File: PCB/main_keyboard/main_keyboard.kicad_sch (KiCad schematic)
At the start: 160 parts

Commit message: Added virtual rows to key matrix #6
The "vritual" rows reduce GPIO usage with matrix from (5+16=21) to (10+8=18)
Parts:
- removed D20, D33, D34, D35, D38, D46, D51, D56, D61, D67, D78, D79: Diode, symbol ScottoKeebs:Placeholder_Diode
- removed S20, S33, S34, S35, S38, S46, S51, S56, S61, S67, S78, S79: Keyswitch, symbol ScottoKeebs:Placeholder_Keyswitch
- D1, D2, D3, D4, D5: footprint (none) -> ScottoKeebs_Components:Diode_DO-35
- D10: renamed from D45; footprint (none) -> ScottoKeebs_Components:Diode_DO-35
- D11: renamed from D6; footprint (none) -> ScottoKeebs_Components:Diode_DO-35
- D12: renamed from D7; footprint (none) -> ScottoKeebs_Components:Diode_DO-35
- D13: renamed from D8; footprint (none) -> ScottoKeebs_Components:Diode_DO-35
- D14: renamed from D9; footprint (none) -> ScottoKeebs_Components:Diode_DO-35
- D15: renamed from D10; footprint (none) -> ScottoKeebs_Components:Diode_DO-35
- D16: renamed from D47; footprint (none) -> ScottoKeebs_Components:Diode_DO-35
- D17: renamed from D48; footprint (none) -> ScottoKeebs_Components:Diode_DO-35
- D18: renamed from D49; footprint (none) -> ScottoKeebs_Components:Diode_DO-35
- D19: renamed from D50; footprint (none) -> ScottoKeebs_Components:Diode_DO-35
- D20: renamed from D11; footprint (none) -> ScottoKeebs_Components:Diode_DO-35
- D21: renamed from D12; footprint (none) -> ScottoKeebs_Components:Diode_DO-35
- D22: renamed from D13; footprint (none) -> ScottoKeebs_Components:Diode_DO-35
- D23: renamed from D14; footprint (none) -> ScottoKeebs_Components:Diode_DO-35
- D24: renamed from D15; footprint (none) -> ScottoKeebs_Components:Diode_DO-35
- D25: renamed from D52; footprint (none) -> ScottoKeebs_Components:Diode_DO-35
- D26: renamed from D53; footprint (none) -> ScottoKeebs_Components:Diode_DO-35
- D27: renamed from D54; footprint (none) -> ScottoKeebs_Components:Diode_DO-35
- D28: renamed from D55; footprint (none) -> ScottoKeebs_Components:Diode_DO-35
- D29: renamed from D16; footprint (none) -> ScottoKeebs_Components:Diode_DO-35
- D30: renamed from D17; footprint (none) -> ScottoKeebs_Components:Diode_DO-35
- D31: renamed from D18; footprint (none) -> ScottoKeebs_Components:Diode_DO-35
- D32: renamed from D19; footprint (none) -> ScottoKeebs_Components:Diode_DO-35
- D33: renamed from D57; footprint (none) -> ScottoKeebs_Components:Diode_DO-35
- D34: renamed from D58; footprint (none) -> ScottoKeebs_Components:Diode_DO-35
- D35: renamed from D59; footprint (none) -> ScottoKeebs_Components:Diode_DO-35
- D36: renamed from D60; footprint (none) -> ScottoKeebs_Components:Diode_DO-35
- D37: renamed from D21; footprint (none) -> ScottoKeebs_Components:Diode_DO-35
- D38: renamed from D22; footprint (none) -> ScottoKeebs_Components:Diode_DO-35
- D39: renamed from D23; footprint (none) -> ScottoKeebs_Components:Diode_DO-35
- D40: renamed from D24; footprint (none) -> ScottoKeebs_Components:Diode_DO-35
- D41: renamed from D25; footprint (none) -> ScottoKeebs_Components:Diode_DO-35
- D42: renamed from D62; footprint (none) -> ScottoKeebs_Components:Diode_DO-35
- D43: renamed from D63; footprint (none) -> ScottoKeebs_Components:Diode_DO-35
- D44: renamed from D64; footprint (none) -> ScottoKeebs_Components:Diode_DO-35
- D45: renamed from D65; footprint (none) -> ScottoKeebs_Components:Diode_DO-35
- D46: renamed from D26; footprint (none) -> ScottoKeebs_Components:Diode_DO-35
- D47: renamed from D27; footprint (none) -> ScottoKeebs_Components:Diode_DO-35
- D48: renamed from D28; footprint (none) -> ScottoKeebs_Components:Diode_DO-35
- D49: renamed from D29; footprint (none) -> ScottoKeebs_Components:Diode_DO-35
- D50: renamed from D30; footprint (none) -> ScottoKeebs_Components:Diode_DO-35
- D51: renamed from D66; footprint (none) -> ScottoKeebs_Components:Diode_DO-35
- D52: renamed from D68; footprint (none) -> ScottoKeebs_Components:Diode_DO-35
- D53: renamed from D69; footprint (none) -> ScottoKeebs_Components:Diode_DO-35
- D54: renamed from D70; footprint (none) -> ScottoKeebs_Components:Diode_DO-35
- D55: renamed from D31; footprint (none) -> ScottoKeebs_Components:Diode_DO-35
- D56: renamed from D32; footprint (none) -> ScottoKeebs_Components:Diode_DO-35
- D57: renamed from D71; footprint (none) -> ScottoKeebs_Components:Diode_DO-35
- D58: renamed from D72; footprint (none) -> ScottoKeebs_Components:Diode_DO-35
- D59: renamed from D73; footprint (none) -> ScottoKeebs_Components:Diode_DO-35
- D6: renamed from D41; footprint (none) -> ScottoKeebs_Components:Diode_DO-35
- D60: renamed from D74; footprint (none) -> ScottoKeebs_Components:Diode_DO-35
- D61: renamed from D75; footprint (none) -> ScottoKeebs_Components:Diode_DO-35
- D62: renamed from D36; footprint (none) -> ScottoKeebs_Components:Diode_DO-35
- D63: renamed from D37; footprint (none) -> ScottoKeebs_Components:Diode_DO-35
- D64: renamed from D39; footprint (none) -> ScottoKeebs_Components:Diode_DO-35
- D65: renamed from D40; footprint (none) -> ScottoKeebs_Components:Diode_DO-35
- D66: renamed from D76; footprint (none) -> ScottoKeebs_Components:Diode_DO-35
- D67: renamed from D77; footprint (none) -> ScottoKeebs_Components:Diode_DO-35
- D68: renamed from D80; footprint (none) -> ScottoKeebs_Components:Diode_DO-35
- D7: renamed from D42; footprint (none) -> ScottoKeebs_Components:Diode_DO-35
- D8: renamed from D43; footprint (none) -> ScottoKeebs_Components:Diode_DO-35
- D9: renamed from D44; footprint (none) -> ScottoKeebs_Components:Diode_DO-35
- renumbered S45 to S10, S6 to S11, S7 to S12, S8 to S13, S9 to S14, S10 to S15, S47 to S16, S48 to S17, S49 to S18, S50 to S19, S11 to S20, S12 to S21, S13 to S22, S14 to S23, S15 to S24, S52 to S25, S53 to S26, S54 to S27, S55 to S28, S16 to S29, S17 to S30, S18 to S31, S19 to S32, S57 to S33, S58 to S34, S59 to S35, S60 to S36, S21 to S37, S22 to S38, S23 to S39, S24 to S40, S25 to S41, S62 to S42, S63 to S43, S64 to S44, S65 to S45, S26 to S46, S27 to S47, S28 to S48, S29 to S49, S30 to S50, S66 to S51, S68 to S52, S69 to S53, S70 to S54, S31 to S55, S32 to S56, S71 to S57, S72 to S58, S73 to S59, S41 to S6, S74 to S60, S75 to S61, S36 to S62, S37 to S63, S39 to S64, S40 to S65, S76 to S66, S77 to S67, S80 to S68, S42 to S7, S43 to S8, S44 to S9
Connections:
- net Col_10 is gone; now on net Col_2: D28.1 (K)
- net Col_11 is gone; now on net Col_3: D36.1 (K)
- net Col_12 is gone; now on net Col_4: D45.1 (K)
- net Col_13 is gone; now on net Col_5: D54.1 (K)
- net Col_14 is gone; now on net Col_6: D61.1 (K)
- net Col_15 is gone; now on net Col_7: D68.1 (K)
- net Col_8 is gone; now on net Col_0: D10.1 (K)
- net Col_9 is gone; now on net Col_1: D19.1 (K)
- net Col_0: no longer D5.1 (K)
- net Col_1: no longer D15.1 (K)
- net Col_2: no longer D24.1 (K)
- net Col_4: no longer D41.1 (K)
- net Col_5: no longer D50.1 (K)
- net Col_7: no longer D65.1 (K)
- net Row_0: no longer S51.1, S57.1, S6.1, S66.1
- net Row_1: no longer S16.1, S25.1, S33.1, S42.1, S58.1, S67.1, S7.1
- net Row_2: now also S13.1, S22.1, S31.1, S39.1, S48.1
- net Row_3: no longer S18.1, S27.1, S35.1, S44.1, S53.1, S60.1, S9.1
- net Row_4: no longer S10.1, S19.1, S28.1, S36.1, S45.1, S54.1, S61.1, S68.1
- net at D32.1 (K): now also D33.2 (A), S33.2
- net Row_7: now reaches S17.1, S26.1, S34.1, S43.1, S52.1, S59.1, S8.1
- net Row_7: no longer S13.1, S22.1, S31.1, S39.1, S48.1
- net at D51.1 (K): now also D52.2 (A), S52.2
- net at D51.2 (A), S51.2: now also D50.1 (K)
- net at D56.1 (K): now also D57.2 (A), S57.2
- net at D66.2 (A), S66.2: now also D65.1 (K)
- net at D25.2 (A), S25.2: now also D24.1 (K)
- net at D6.2 (A), S6.2: now also D5.1 (K)
- net at D63.1 (K): now also D64.2 (A), S64.2
- net at D67.1 (K): now also D68.2 (A), S68.2
- net at D42.2 (A), S42.2: now also D41.1 (K)
- net at D16.2 (A), S16.2: now also D15.1 (K)
- new net Row_5: S51.1, S57.1, S6.1, S66.1
- new net Row_6: S16.1, S25.1, S33.1, S42.1, S58.1, S67.1, S7.1
- new net Row_8: S18.1, S27.1, S35.1, S44.1, S53.1, S60.1, S9.1
- new net Row_9: S10.1, S19.1, S28.1, S36.1, S45.1, S54.1, S61.1, S68.1
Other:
- note added: "I2C interface"
- note added: "Keyboard switches"
- note added: "Microcontroller"
- moved on the sheet: D1, D10, D11, D12, D13, D14, D15, D16, D17, D18, D19, D2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

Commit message: Layout partial completion
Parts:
- removed D66, D67, D68: Diode, ScottoKeebs_Components:Diode_DO-35, symbol ScottoKeebs:Placeholder_Diode
- removed S66, S67, S68: Keyswitch, symbol ScottoKeebs:Placeholder_Keyswitch
- added C1, C2, C3, C4: 0.1u, symbol Device:C_Small
- added C5: 4.7u, symbol Device:C_Small
- added C6: C_Small (1uF?), symbol Device:C_Small
- added C7, C8: c_small, symbol Device:C_Small
- added D100, D101, D102, D103, D104, D105, D106, D107, D108, D109, D110, D111, D112, D113, D114, D115, D116, D117, D118, D119, D120, D121, D122, D123, D124, D125, D126, D127, D128, D129, D130, D131, D132, D133, D134, D135, D69, D71, D72, D73, D74, D75, D76, D77, D78, D79, D80, D81, D82, D83, D84, D85, D86, D87, D88, D89, D90, D91, D92, D93, D94, D95, D96, D97, D98, D99: LED_SK6812MINI, ScottoKeebs_Components:LED_SK6812MINI, symbol ScottoKeebs:LED_SK6812MINI
- added D70: Diode, ScottoKeebs_Components:Diode_SOD-123, symbol ScottoKeebs:Placeholder_Diode
- added J1: Conn_01x05_Pin, Connector:FanPinHeader_1x03_P2.54mm_Vertical, symbol Connector:Conn_01x05_Pin
- added J2: Conn_01x04_Pin, symbol Connector:Conn_01x04_Pin
- added R1, R2: R, symbol Device:R
- added R3, R4: R_Small, symbol Device:R_Small
- added S69: Keyswitch, ScottoKeebs_Hotswap:Hotswap_MX_Plated_2.25u, symbol ScottoKeebs:Placeholder_Keyswitch
- added SW1: SW_Push, symbol Switch:SW_Push
- added U1: ATmega32U4-A, Package_QFP:TQFP-44_10x10mm_P0.8mm, symbol MCU_Microchip_ATmega:ATmega32U4-A
- added Y1: Crystal 8MHz, symbol Device:Crystal
- D1, D10, D11, D12, D13, D14, D15, D16, D17, D18, D19, D2, D20, D21, D22, D23, D24, D25, D26, D27, D28, D29, D3, D30, D31, D32, D33, D34, D35, D36, D37, D38, D39, D4, D40, D41, D42, D43, D44, D45, D46, D47, D48, D49, D5, D50, D51, D52, D53, D54, D55, D56, D57, D58, D59, D6, D60, D61, D62, D63, D64, D65, D7, D8, D9: footprint ScottoKeebs_Components:Diode_DO-35 -> ScottoKeebs_Components:Diode_SOD-123
- S1, S10, S11, S12, S13, S14, S16, S17, S18, S19, S20, S21, S22, S23, S25, S26, S27, S28, S29, S30, S31, S32, S33, S34, S35, S36, S37, S38, S39, S40, S42, S43, S44, S45, S46, S47, S48, S49, S51, S53, S54, S55, S56, S57, S59, S60, S61, S62, S63, S64, S7, S8, S9: footprint (none) -> ScottoKeebs_Hotswap:Hotswap_MX_Plated_1.00u
- S15, S4, S58: footprint (none) -> ScottoKeebs_Hotswap:Hotswap_MX_Plated_2.25u
- S2: footprint (none) -> ScottoKeebs_Hotswap:Hotswap_MX_Plated_1.50u
- S24, S3: footprint (none) -> ScottoKeebs_Hotswap:Hotswap_MX_Plated_1.75u
- S41, S5, S50, S52, S6: footprint (none) -> ScottoKeebs_Hotswap:Hotswap_MX_Plated_1.25u
- S65: footprint (none) -> ScottoKeebs_Hotswap:Hotswap_MX_Plated_2.00u
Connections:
- net Col_5: now also D55.1 (K); no longer D54.1 (K)
- net Col_6: now also D65.1 (K); no longer D61.1 (K)
- net GND: now also C1.1, C2.1, C3.1, C4.1, C5.1, C6.2, C7.2, C8.2, D100.3 (GND), D101.3 (GND), D102.3 (GND), D103.3 (GND), D104.3 (GND), D105.3 (GND), D106.3 (GND), D107.3 (GND), D108.3 (GND), D109.3 (GND), D110.3 (GND), D111.3 (GND), D112.3 (GND), D113.3 (GND), D114.3 (GND), D115.3 (GND), D116.3 (GND), D117.3 (GND), D118.3 (GND), D119.3 (GND), D120.3 (GND), D121.3 (GND), D122.3 (GND), D123.3 (GND), D124.3 (GND), D125.3 (GND), D126.3 (GND), D127.3 (GND), D128.3 (GND), D129.3 (GND), D130.3 (GND), D131.3 (GND), D132.3 (GND), D133.3 (GND), D134.3 (GND), D135.3 (GND), D69.3 (GND), D71.3 (GND), D72.3 (GND), D73.3 (GND), D74.3 (GND), D75.3 (GND), D76.3 (GND), D77.3 (GND), D78.3 (GND), D79.3 (GND), D80.3 (GND), D81.3 (GND), D82.3 (GND), D83.3 (GND), D84.3 (GND), D85.3 (GND), D86.3 (GND), D87.3 (GND), D88.3 (GND), D89.3 (GND), D90.3 (GND), D91.3 (GND), D92.3 (GND), D93.3 (GND), D94.3 (GND), D95.3 (GND), D96.3 (GND), D97.3 (GND), D98.3 (GND), D99.3 (GND), J1.1 (Pin_1), J2.4 (Pin_4), R4.2, SW1.1, U1.15 (GND), U1.23 (GND), U1.35 (GND), U1.43 (GND), U1.5 (UGND)
- net Row_0: now also S56.1; no longer S55.1, S62.1
- net Row_1: now also S57.1; no longer S56.1, S63.1
- net Row_2: now also S58.1
- net Row_3: now also S59.1; no longer S64.1
- net Row_4: now also S60.1; no longer S24.1, S65.1
- net Row_5: now also S24.1, S61.1, S69.1; no longer S57.1
- net Row_6: now also S52.1, S62.1; no longer S58.1
- net Row_7: now also S53.1, S63.1; no longer S52.1, S59.1
- net Row_8: now also S54.1, S64.1; no longer S53.1, S60.1
- net Row_9: now also S55.1, S65.1; no longer S54.1, S61.1
- net SCL: now also J1.3 (Pin_3), R2.2, U1.18 (PD0)
- net SDA: now also J1.4 (Pin_4), R1.2, U1.19 (PD1)
- net SINT: now also J1.2 (Pin_2)
- net at D33.2 (A), S33.2: now also D70.1 (K); no longer D32.1 (K)
- net at D58.1 (K), D59.2 (A), S59.2: now also D59.1 (K), D60.1 (K), D60.2 (A), D61.2 (A), S60.2, S61.2
- net at D55.2 (A), S55.2: now also D54.1 (K)
- net at D56.2 (A), S56.2: no longer D55.1 (K)
- net at D62.2 (A), S62.2: now also D61.1 (K)
- new net: D32.1 (K), D70.2 (A), S69.2
- new net: D133.2 (DOUT), D134.4 (DIN)
- new net: D131.2 (DOUT), D133.4 (DIN)
- new net: D117.2 (DOUT), D119.4 (DIN)
- new net: D115.2 (DOUT), D117.4 (DIN)
- new net: D134.2 (DOUT), D135.4 (DIN)
- new net: D107.2 (DOUT), D109.4 (DIN)
- new net: D105.2 (DOUT), D107.4 (DIN)
- new net: D108.2 (DOUT), D110.4 (DIN)
- new net: D106.2 (DOUT), D108.4 (DIN)
- new net: D128.2 (DOUT), D130.4 (DIN)
- new net: D126.2 (DOUT), D128.4 (DIN)
- new net: D74.2 (DOUT), D75.4 (DIN)
- new net: D73.2 (DOUT), D74.4 (DIN)
- new net: D93.2 (DOUT), D94.4 (DIN)
- new net: D92.2 (DOUT), D93.4 (DIN)
- new net: D91.2 (DOUT), D92.4 (DIN)
- new net: D75.2 (DOUT), D76.4 (DIN)
- new net: C8.1, U1.16 (XTAL2), Y1.2
- new net: C7.1, U1.17 (XTAL1), Y1.1
- new net: U1.2 (UVCC), U1.24 (AVCC), U1.44 (AVCC)
- new net: R4.1, U1.33 (~{HWB}/PE2)
- new net: C6.1, U1.6 (UCAP)
- new net: D111.2 (DOUT), D113.4 (DIN)
- new net: D109.2 (DOUT), D111.4 (DIN)
- new net: D112.2 (DOUT), D114.4 (DIN)
- new net: D110.2 (DOUT), D112.4 (DIN)
- new net: D87.2 (DOUT), D88.4 (DIN)
- new net: D86.2 (DOUT), D87.4 (DIN)
- new net: D81.2 (DOUT), D82.4 (DIN)
- new net: D80.2 (DOUT), D81.4 (DIN)
- new net: D69.2 (DOUT), D71.4 (DIN)
- new net: D90.2 (DOUT), D91.4 (DIN)
- new net: D89.2 (DOUT), D90.4 (DIN)
- new net: D129.2 (DOUT), D131.4 (DIN)
- new net: D85.2 (DOUT), D86.4 (DIN)
- new net: D82.2 (DOUT), D83.4 (DIN)
- new net: D84.2 (DOUT), D85.4 (DIN)
- new net: D83.2 (DOUT), D84.4 (DIN)
- new net: D101.2 (DOUT), D102.4 (DIN)
- new net: D100.2 (DOUT), D101.4 (DIN)
- new net: D125.2 (DOUT), D127.4 (DIN)
- new net: D123.2 (DOUT), D125.4 (DIN)
- new net: D127.2 (DOUT), D129.4 (DIN)
- new net: D121.2 (DOUT), D123.4 (DIN)
- new net: D77.2 (DOUT), D78.4 (DIN)
- new net: D76.2 (DOUT), D77.4 (DIN)
- new net: D122.2 (DOUT), D124.4 (DIN)
- new net: D120.2 (DOUT), D122.4 (DIN)
- new net: D113.2 (DOUT), D115.4 (DIN)
- new net: D88.2 (DOUT), D89.4 (DIN)
- new net: D124.2 (DOUT), D126.4 (DIN)
- new net: D95.2 (DOUT), D96.4 (DIN)
- new net: D94.2 (DOUT), D95.4 (DIN)
- new net: D79.2 (DOUT), D80.4 (DIN)
- new net: D78.2 (DOUT), D79.4 (DIN)
- new net: D103.2 (DOUT), D105.4 (DIN)
- new net: D103.4 (DIN), D132.2 (DOUT)
- new net: D98.2 (DOUT), D99.4 (DIN)
- new net: D97.2 (DOUT), D98.4 (DIN)
- new net: D116.2 (DOUT), D118.4 (DIN)
- new net: D114.2 (DOUT), D116.4 (DIN)
- new net: D118.2 (DOUT), D120.4 (DIN)
- new net: D71.2 (DOUT), D72.4 (DIN)
- new net: D102.2 (DOUT), D104.4 (DIN)
- new net: D96.2 (DOUT), D97.4 (DIN)
- new net: D130.2 (DOUT), D132.4 (DIN)
- new net: D104.2 (DOUT), D106.4 (DIN)
- new net: D72.2 (DOUT), D73.4 (DIN)
- new net: D119.2 (DOUT), D121.4 (DIN)
- new net: D100.4 (DIN), D99.2 (DOUT)
- new net +3V3: R1.1, R2.1
- new net +5V: C1.2, C2.2, C3.2, C4.2, C5.2, D100.1 (VDD), D101.1 (VDD), D102.1 (VDD), D103.1 (VDD), D104.1 (VDD), D105.1 (VDD), D106.1 (VDD), D107.1 (VDD), D108.1 (VDD), D109.1 (VDD), D110.1 (VDD), D111.1 (VDD), D112.1 (VDD), D113.1 (VDD), D114.1 (VDD), D115.1 (VDD), D116.1 (VDD), D117.1 (VDD), D118.1 (VDD), D119.1 (VDD), D120.1 (VDD), D121.1 (VDD), D122.1 (VDD), D123.1 (VDD), D124.1 (VDD), D125.1 (VDD), D126.1 (VDD), D127.1 (VDD), D128.1 (VDD), D129.1 (VDD), D130.1 (VDD), D131.1 (VDD), D132.1 (VDD), D133.1 (VDD), D134.1 (VDD), D135.1 (VDD), D69.1 (VDD), D71.1 (VDD), D72.1 (VDD), D73.1 (VDD), D74.1 (VDD), D75.1 (VDD), D76.1 (VDD), D77.1 (VDD), D78.1 (VDD), D79.1 (VDD), D80.1 (VDD), D81.1 (VDD), D82.1 (VDD), D83.1 (VDD), D84.1 (VDD), D85.1 (VDD), D86.1 (VDD), D87.1 (VDD), D88.1 (VDD), D89.1 (VDD), D90.1 (VDD), D91.1 (VDD), D92.1 (VDD), D93.1 (VDD), D94.1 (VDD), D95.1 (VDD), D96.1 (VDD), D97.1 (VDD), D98.1 (VDD), D99.1 (VDD), J1.5 (Pin_5), J2.1 (Pin_1), R3.1, U1.14 (VCC), U1.34 (VCC)
- new net LED_DIN: D69.4 (DIN)
- new net RST: R3.2, SW1.2, U1.13 (~{RESET})
- new net RX: U1.20 (PD2)
- new net TX: U1.21 (PD3)
- new net USB_D+: J2.3 (Pin_3), U1.4 (D+)
- new net USB_D-: J2.2 (Pin_2), U1.3 (D-)
- no-connect marks 0 -> 1
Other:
- note added: "Clock"
- note added: "External I/O"
- note added: "I2C"
- note added: "Uniefied Daughter board"
- note removed: "I2C interface"
- moved on the sheet: D1, D10, D11, D12, D13, D14, D15, D16, D17, D18, D19, D2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

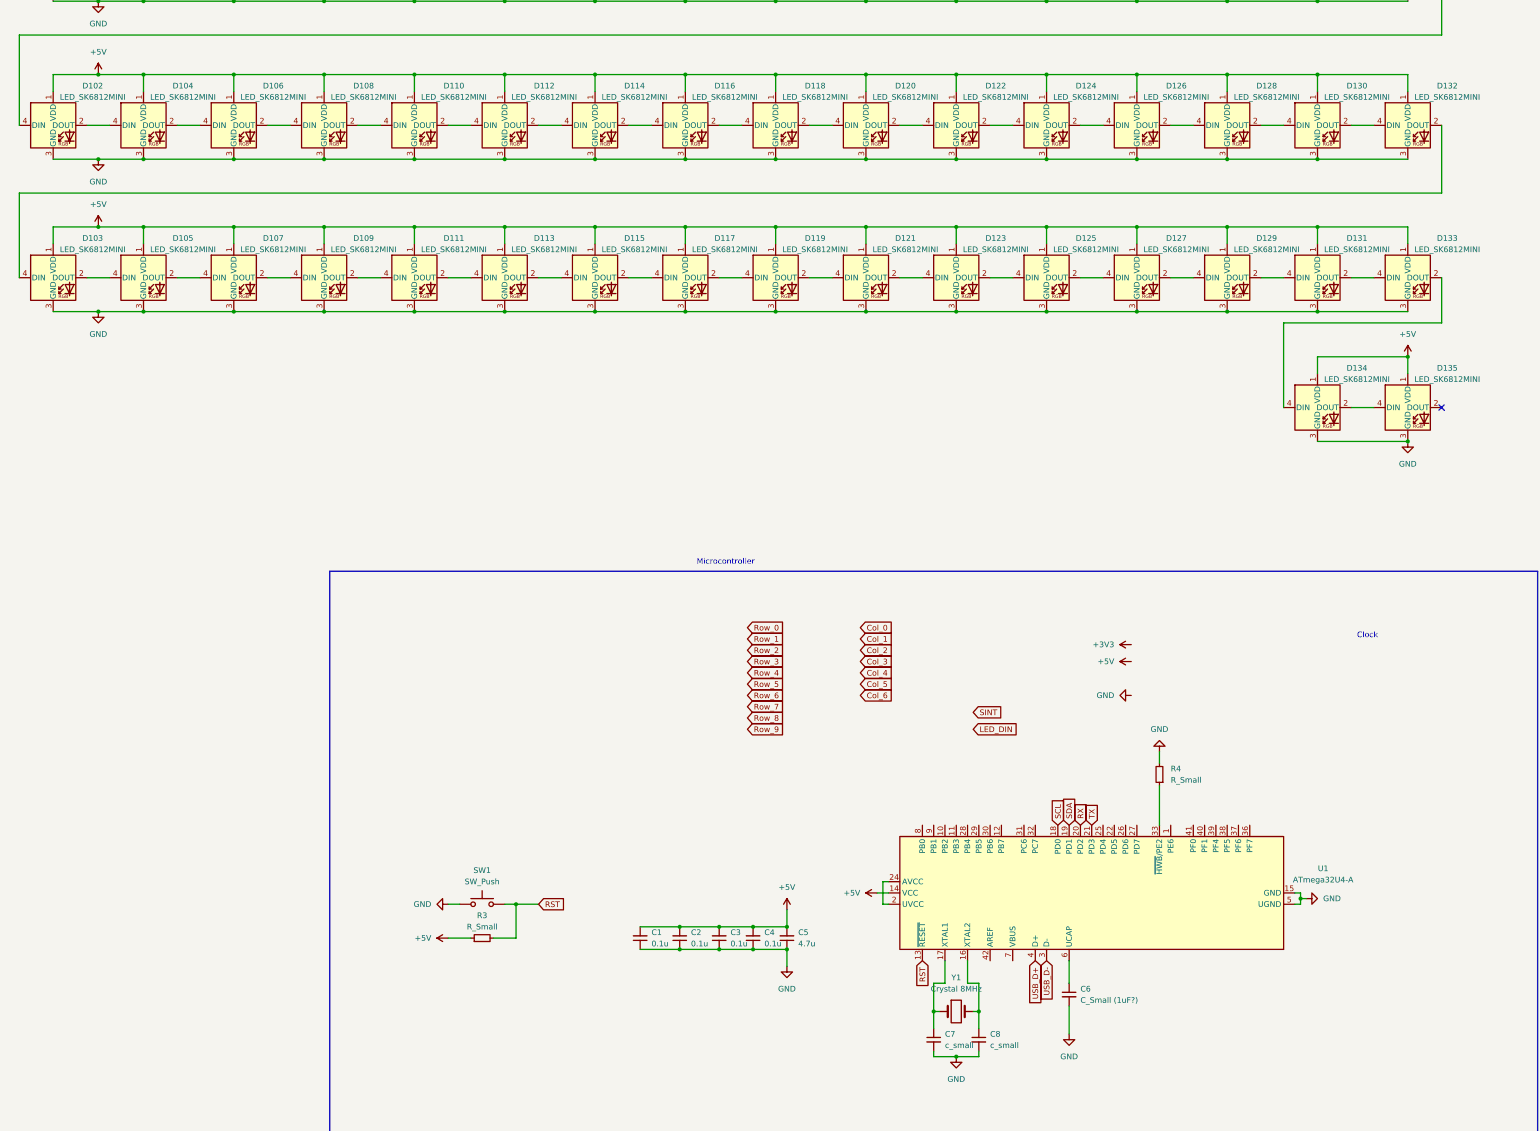
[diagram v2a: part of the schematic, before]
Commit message: leds placed
smd led footprints placed
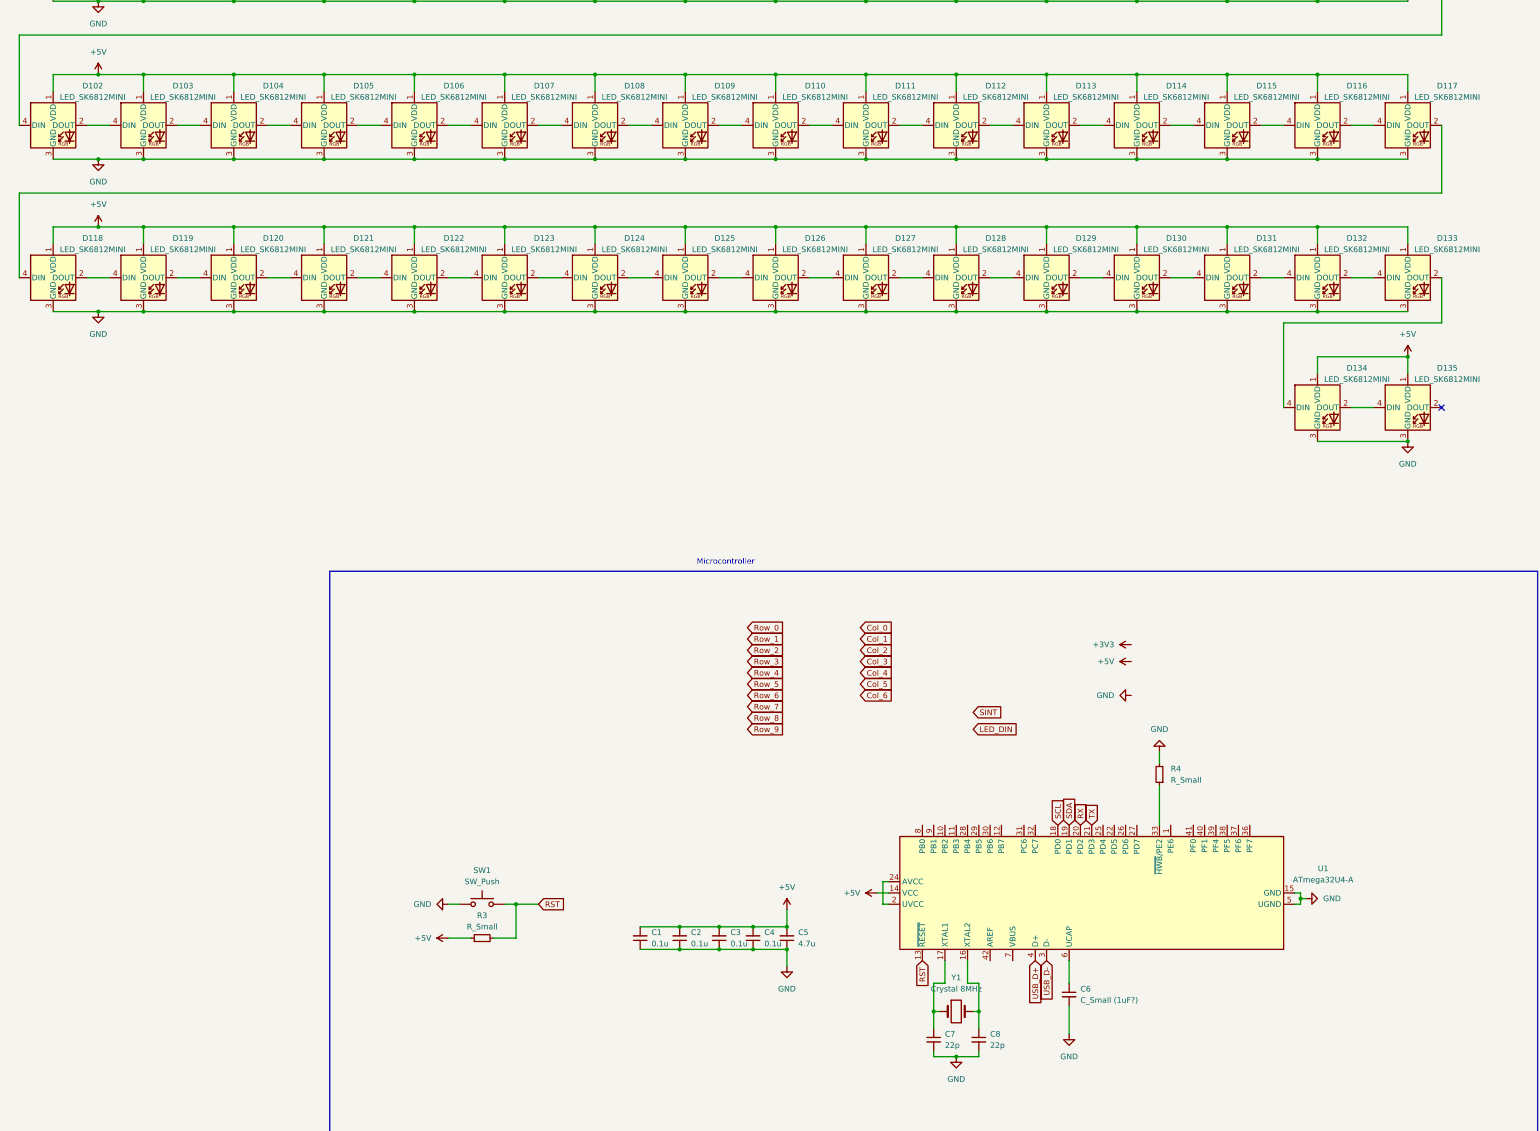
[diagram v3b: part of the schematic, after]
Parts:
- C1, C2, C3, C4: footprint (none) -> Capacitor_SMD:C_01005_0402Metric_Pad0.57x0.30mm_HandSolder
- C5: footprint (none) -> Capacitor_SMD:C_0201_0603Metric_Pad0.64x0.40mm_HandSolder
- C7, C8: value c_small -> 22p; footprint (none) -> Capacitor_SMD:C_01005_0402Metric_Pad0.57x0.30mm_HandSolder
- S64: footprint ScottoKeebs_Hotswap:Hotswap_MX_Plated_1.00u -> ScottoKeebs_Hotswap:Hotswap_MX_Plated_1.50u
- renumbered D104 to D103, D106 to D104, D108 to D105, D110 to D106, D112 to D107, D114 to D108, D116 to D109, D118 to D110, D120 to D111, D122 to D112, D124 to D113, D126 to D114, D128 to D115, D130 to D116, D132 to D117, D103 to D118, D105 to D119, D107 to D120, D109 to D121, D111 to D122, D113 to D123, D115 to D124, D117 to D125, D119 to D126, D121 to D127, D123 to D128, D125 to D129, D127 to D130, D129 to D131, D131 to D132
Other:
- note removed: "Clock"

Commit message: First draft Main board
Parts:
- C1, C2, C3, C4, C7, C8: footprint Capacitor_SMD:C_01005_0402Metric_Pad0.57x0.30mm_HandSolder -> Capacitor_SMD:C_0805_2012Metric_Pad1.18x1.45mm_HandSolder
- C5: footprint Capacitor_SMD:C_0201_0603Metric_Pad0.64x0.40mm_HandSolder -> Capacitor_SMD:C_0603_1608Metric_Pad1.08x0.95mm_HandSolder
- C6: footprint (none) -> Capacitor_SMD:C_0603_1608Metric_Pad1.08x0.95mm_HandSolder
- J1: footprint Connector:FanPinHeader_1x03_P2.54mm_Vertical -> Connector_PinHeader_2.54mm:PinHeader_1x05_P2.54mm_Vertical
- J2: footprint (none) -> Connector_JST:JST_EH_S4B-EH_1x04_P2.50mm_Horizontal
- R3, R4: value R_Small -> 10k; footprint (none) -> Resistor_SMD:R_0805_2012Metric_Pad1.20x1.40mm_HandSolder
- SW1: footprint (none) -> Connector_PinHeader_1.00mm:PinHeader_1x02_P1.00mm_Vertical
- Y1: footprint (none) -> Crystal:Crystal_HC18-U_Vertical
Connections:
- net +5V: now also U1.24 (AVCC), U1.44 (AVCC); no longer C5.2
- net Col_0: now also U1.32 (PC7)
- net Col_1: now also U1.36 (PF7)
- net Col_2: now also U1.37 (PF6)
- net Col_3: now also U1.38 (PF5)
- net Col_4: now also U1.39 (PF4)
- net Col_5: now also U1.40 (PF1)
- net Col_6: now also U1.41 (PF0)
- net GND: now also C5.2; no longer C5.1
- net LED_DIN: now also U1.8 (PB0)
- net Row_0: now also U1.10 (PB2)
- net Row_1: now also U1.31 (PC6)
- net Row_2: now also U1.29 (PB5)
- net Row_3: now also U1.27 (PD7)
- net Row_4: now also U1.25 (PD4)
- net Row_5: now also U1.26 (PD6)
- net Row_6: now also U1.9 (PB1)
- net Row_7: now also U1.1 (PE6)
- net Row_8: now also U1.30 (PB6)
- net Row_9: now also U1.28 (PB4)
- net XTAL_P: now reaches C8.1, U1.16 (XTAL2), Y1.2
- net XTAL_N: now reaches C7.1, U1.17 (XTAL1), Y1.1
- net RX renamed RX+
- net TX renamed TX-
- new net: D58.1 (K), D59.2 (A), S59.2
- new net: D59.1 (K), D60.2 (A), S60.2
- new net: C5.1, U1.2 (UVCC)
- new net: D60.1 (K), D61.2 (A), S61.2
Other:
- moved on the sheet: C5
